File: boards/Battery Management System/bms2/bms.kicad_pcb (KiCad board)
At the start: 2 copper layers, 28 parts, among them J2 1986660-2, J3 B5B-XH-A, U1 BD48L32G, U2 BD48L32G, U3 BD48L32G, U4 BD48L32G, U5 SN74HC08DR

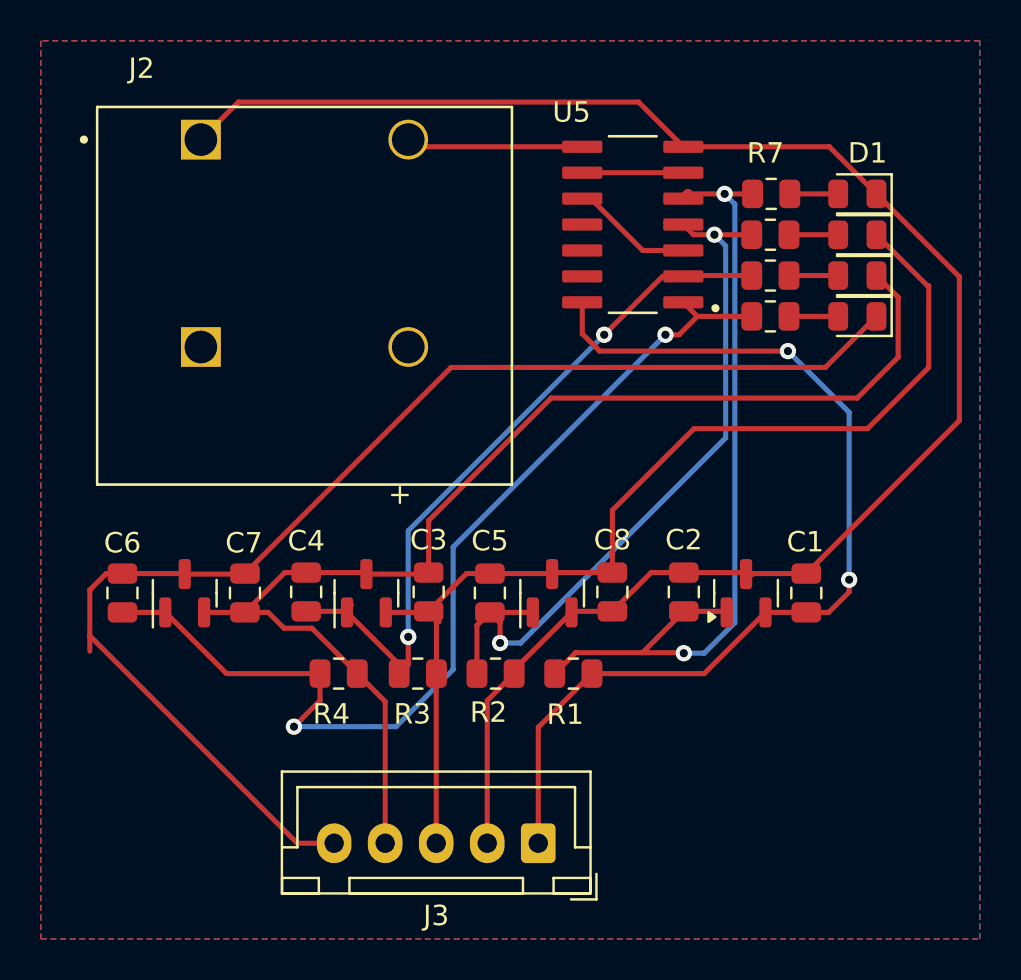
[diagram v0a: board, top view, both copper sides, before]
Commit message: flipped battery terminal on BMS PCB
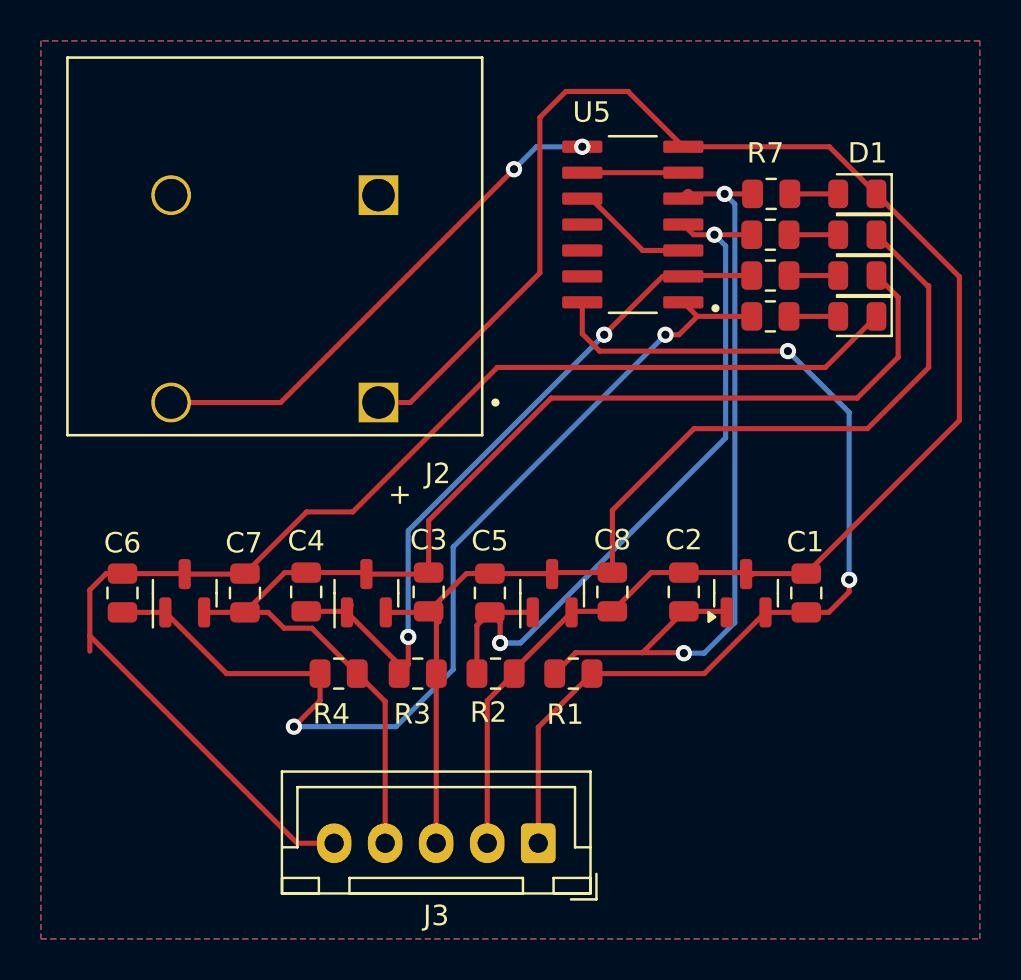
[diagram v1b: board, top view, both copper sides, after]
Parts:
- moved J2 15.5 mm to (36.5, 45.7), turned to 180 degrees
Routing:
- net /V_OUT: track 8.67 -> 25.3 mm, vias 0 -> 2
- net /V_CELL_2: track 84.8 -> 86.0 mm
